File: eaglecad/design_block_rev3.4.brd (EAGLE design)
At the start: 160 x 100 mm, 69 parts, among them Q1 MOSFET-PCH-SOT23-6, Q2 MOSFET-PCH-SOT23-6, Q3 PMV45EN, Q4 PMV45EN, Q5 DMP2240UDM, U1 MAX4211FETE, U2 MAX7310ATE, U3 MIC842LYC5, U4 MIC842LYC5

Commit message: power domain updates
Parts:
- moved R11 68.0 mm to (48.0, 15.0)
- moved TP13 67.8 mm to (45.0, 10.0)
- moved R20 66.7 mm to (48.0, 12.0), turned to 180 degrees
- moved Q3 65.9 mm to (48.0, 19.0), turned to 0 degrees
- moved R2 58.8 mm to (51.0, 22.0), turned to 0 degrees
- moved Q1 58.4 mm to (51.0, 26.0), turned to 270 degrees
- moved D2 57.8 mm to (52.0, 16.0), turned to 90 degrees
- moved TP9 56.7 mm to (39.0, 15.0)
- moved R3 54.8 mm to (42.0, 11.0), turned to 0 degrees
- moved Q4 50.0 mm to (34.0, 14.0), turned to 90 degrees
- moved C1 49.8 mm to (43.0, 33.0)
- moved C2 49.8 mm to (33.0, 33.0), turned to 0 degrees
- moved Q2 49.8 mm to (42.0, 14.0), turned to 270 degrees
- moved R1 49.8 mm to (48.0, 31.0)
- moved R10 49.8 mm to (33.0, 30.0)
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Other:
- board outline removed

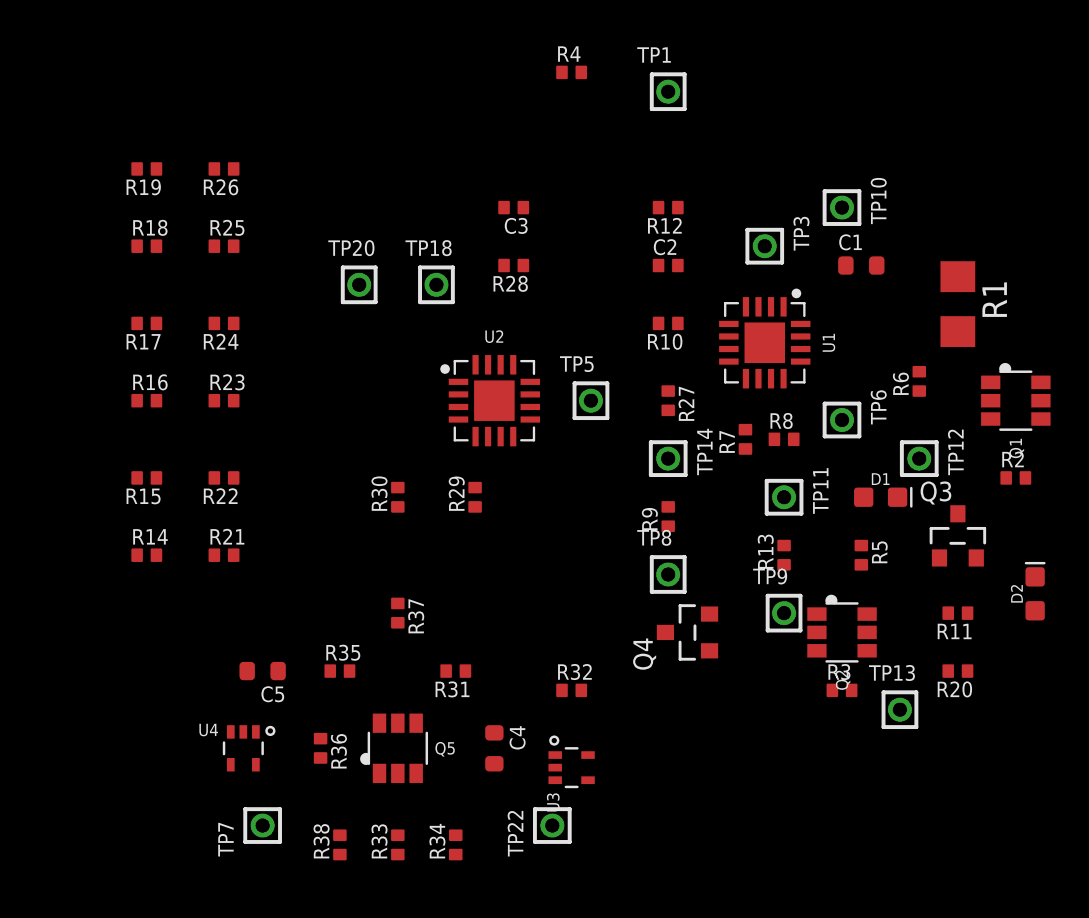
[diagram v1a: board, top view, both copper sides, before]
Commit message: ACS power domaine routing in progress
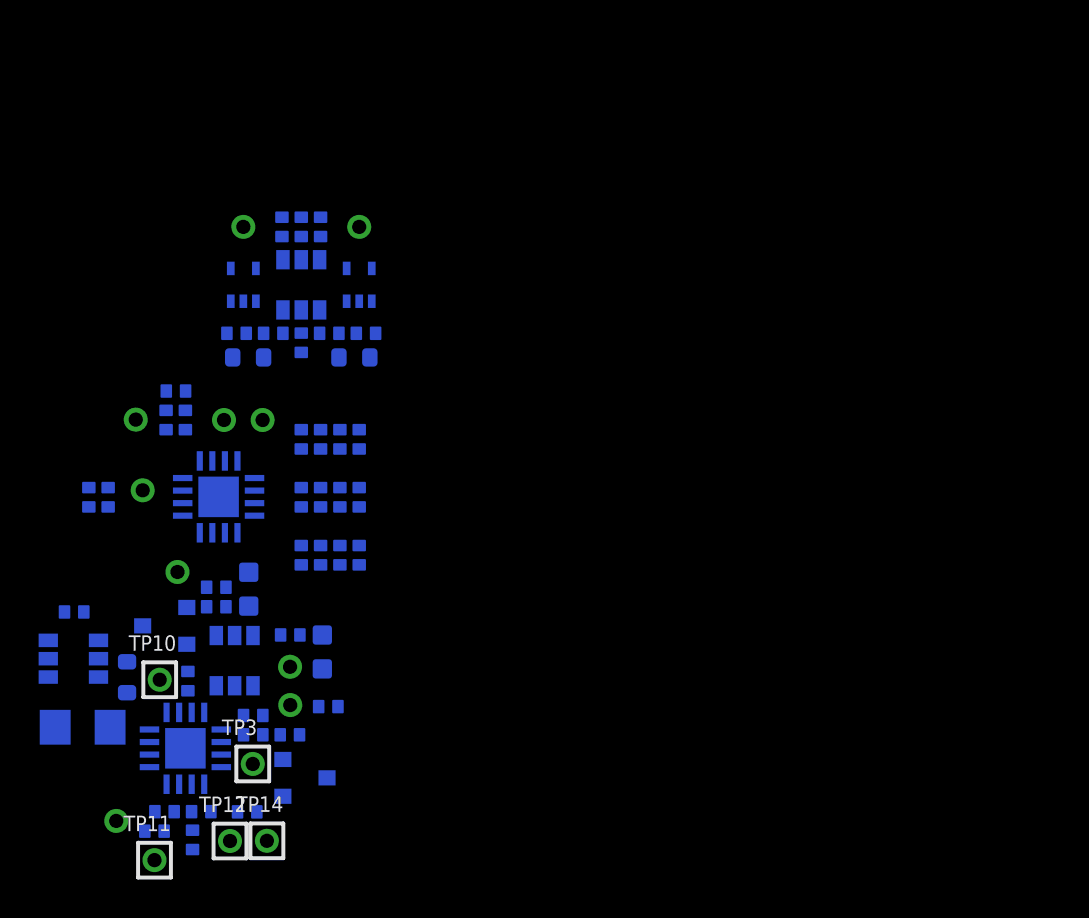
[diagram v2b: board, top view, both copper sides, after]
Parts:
- moved Q1 50.6 mm to (2.20, 12.6), flipped to the bottom, turned to 90 degrees
- moved R1 50.3 mm to (2.68, 9.09), flipped to the bottom, turned to 180 degrees
- moved R2 49.3 mm to (2.24, 15.1), flipped to the bottom, turned to 180 degrees
- moved R6 44.5 mm to (8.37, 3.26), flipped to the bottom, turned to 270 degrees
- moved C1 43.6 mm to (4.98, 11.7), flipped to the bottom, turned to 90 degrees
- moved TP10 43.0 mm to (6.67, 11.6), turned to 0 degrees
- moved TP6 42.9 mm to (4.42, 4.24), flipped to the bottom
- moved Q3 41.3 mm to (6.93, 14.3), flipped to the bottom, turned to 270 degrees
- moved TP12 40.8 mm to (10.3, 3.20), turned to 0 degrees
- moved D2 40.7 mm to (11.3, 16.2), flipped to the bottom, turned to 270 degrees
- moved R20 38.6 mm to (9.60, 16.3), flipped to the bottom, turned to 0 degrees
- moved R11 38.4 mm to (9.60, 15.3), flipped to the bottom, turned to 0 degrees
- moved TP13 38.1 mm to (7.59, 17.1), flipped to the bottom
- moved TP3 37.7 mm to (11.5, 7.19), turned to 0 degrees
- moved TP11 37.6 mm to (6.40, 2.21), turned to 0 degrees
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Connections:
- net IOUT renamed IOUT_Q_
- net POUT renamed POUT_Q_
